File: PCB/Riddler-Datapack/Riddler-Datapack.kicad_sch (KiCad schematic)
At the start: 0 parts

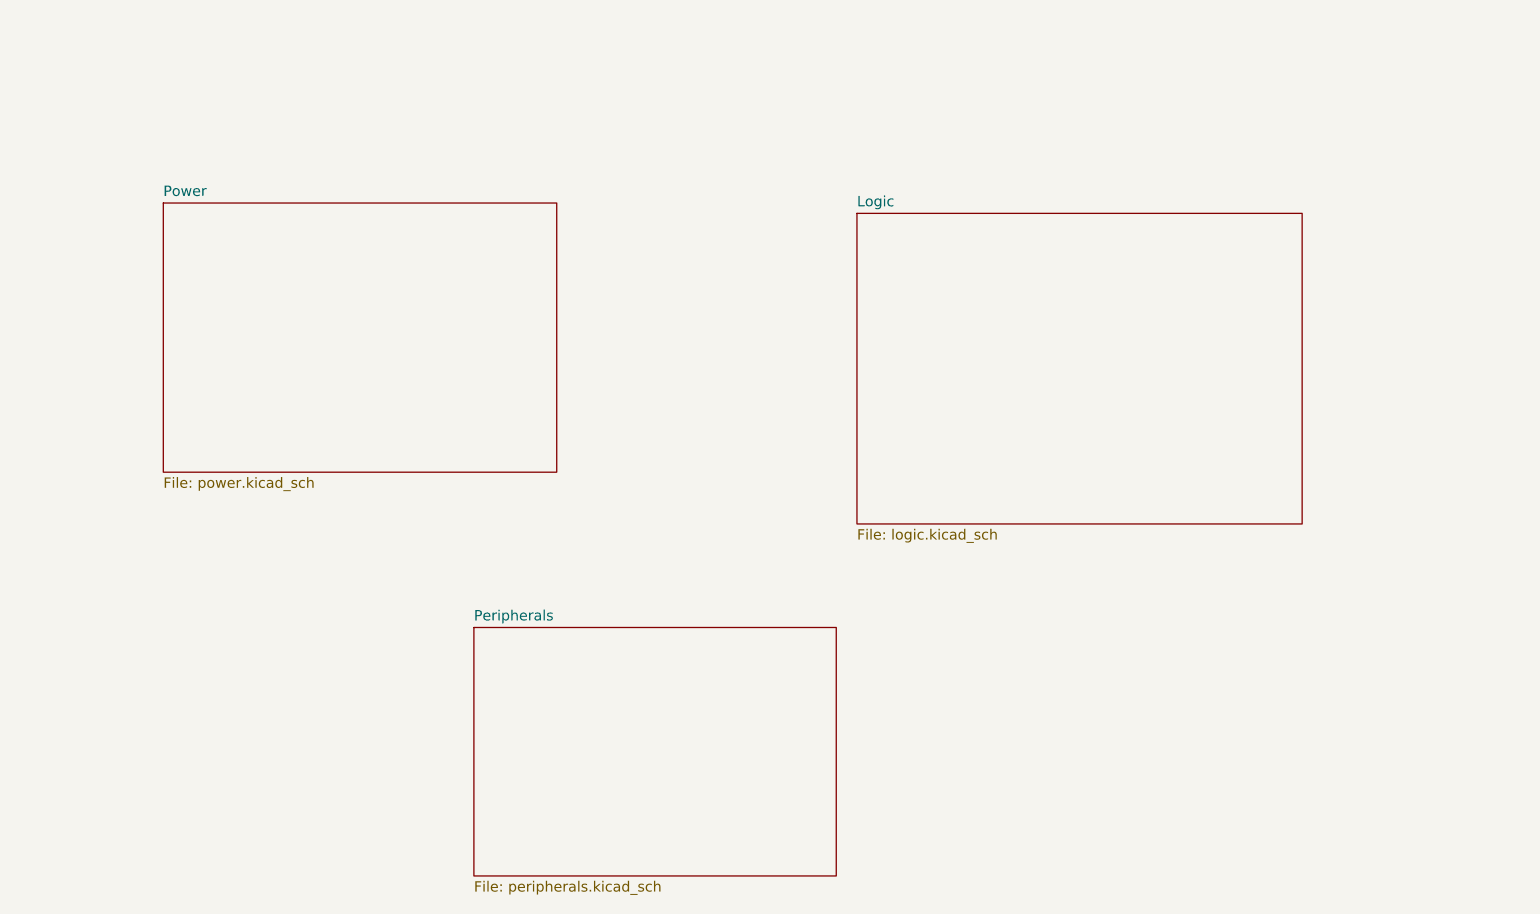
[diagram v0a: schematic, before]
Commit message: Complete schematics v0.5, add schematic PDF export and active prop reference
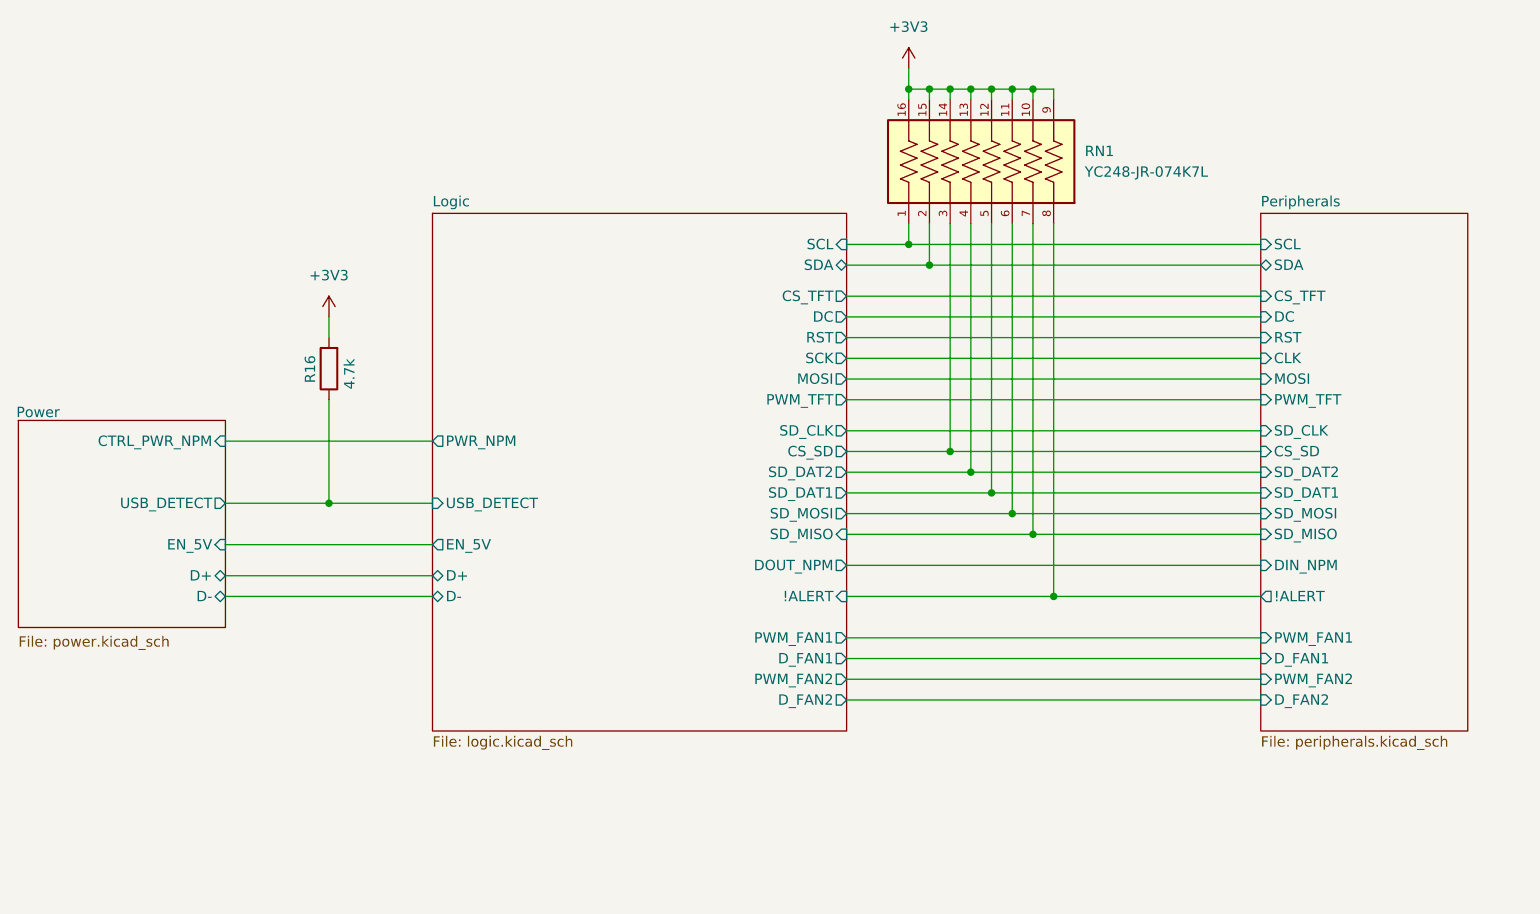
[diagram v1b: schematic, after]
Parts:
- added R16: 4.7k, Resistor_SMD:R_0402_1005Metric, symbol Device:R
- added RN1: YC248-JR-074K7L, YC248-JR-074K7L:RESCAXS50P400X160X55-16N, symbol YC248-JR-074K7L:YC248-JR-074K7L
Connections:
- new net +3V3: R16.2, RN1.10, RN1.11, RN1.12, RN1.13, RN1.14, RN1.15, RN1.16, RN1.9
- new net Logic/!ALERT: RN1.8
- new net Logic/CS_SD: RN1.3
- new net Logic/SCL: RN1.1
- new net Logic/SDA: RN1.2
- new net Logic/SD_DAT1: RN1.5
- new net Logic/SD_DAT2: RN1.4
- new net Logic/SD_MISO: RN1.7
- new net Logic/SD_MOSI: RN1.6
- new net Logic/USB_DETECT: R16.1
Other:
- sheet Logic ports: added !ALERT, CS_SD, CS_TFT, D+, D-, DC, DOUT_NPM, D_FAN1, D_FAN2, EN_5V, MOSI, PWM_FAN1, PWM_FAN2, PWM_TFT, PWR_NPM, RST, SCK, SCL, SDA, SD_CLK, SD_DAT1, SD_DAT2, SD_MISO, SD_MOSI, USB_DETECT; removed none
- sheet Peripherals ports: added !ALERT, CLK, CS_SD, CS_TFT, DC, DIN_NPM, D_FAN1, D_FAN2, MOSI, PWM_FAN1, PWM_FAN2, PWM_TFT, RST, SCL, SDA, SD_CLK, SD_DAT1, SD_DAT2, SD_MISO, SD_MOSI; removed none
- sheet Power ports: added CTRL_PWR_NPM, D+, D-, EN_5V, USB_DETECT; removed none
